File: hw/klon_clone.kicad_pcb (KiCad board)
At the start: 2 copper layers, 0 parts

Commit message: Updated J1/J3 footprints and symbols. Initial layout placement.
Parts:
- added C1: 100n, Capacitor_THT:C_Rect_L13.0mm_W5.0mm_P10.00mm_FKS3_FKP3_MKS4, F.Cu at (118.0, 116.5)
- added C10: 1u, Capacitor_SMD:C_0805_2012Metric_Pad1.18x1.45mm_HandSolder, F.Cu at (181.0, 122.5)
- added C11: 1u, kicad_footprint_library:C_Axial_L17.5mm_W7.8mm_P7.5mm_Horizontal, F.Cu at (130.5, 119.5)
- added C12: 1u, Capacitor_SMD:C_0805_2012Metric_Pad1.18x1.45mm_HandSolder, F.Cu at (172.0, 118.0)
- added C13: 82n, Capacitor_THT:C_Rect_L10.3mm_W5.0mm_P7.50mm_MKS4, F.Cu at (116.3, 102.5)
- added C14: 390p, Capacitor_THT:C_Rect_L10.0mm_W4.0mm_P7.50mm_MKS4, F.Cu at (109.2, 96.5)
- added C15: 1u, kicad_footprint_library:C_Axial_L17.5mm_W7.8mm_P7.5mm_Horizontal, F.Cu at (97.5, 94.5)
- added C16: 47u, Capacitor_THT:CP_Radial_D8.0mm_P5.00mm, F.Cu at (189.1, 104.0)
- added C17: 1u, kicad_footprint_library:C_Axial_L17.5mm_W7.8mm_P7.5mm_Horizontal, F.Cu at (112.0, 84.0)
- added C18: 2.2n, Capacitor_THT:C_Rect_L18.0mm_W7.0mm_P15.00mm_FKS3_FKP3, F.Cu at (119.5, 89.0)
- added C19: 27n, Capacitor_THT:C_Rect_L10.3mm_W4.5mm_P7.50mm_MKS4, F.Cu at (119.5, 82.5)
- added C2: 1u, Capacitor_SMD:C_0805_2012Metric_Pad1.18x1.45mm_HandSolder, F.Cu at (182.0, 102.0)
- added C20: 820p, Capacitor_THT:C_Rect_L13.0mm_W4.0mm_P10.00mm_FKS3_FKP3_MKS4, F.Cu at (119.5, 68.0)
- added C21: 3.9n, Capacitor_THT:C_Rect_L16.5mm_W5.0mm_P15.00mm_MKT, F.Cu at (141.5, 72.0)
- added C22: 4.7u, Capacitor_THT:CP_Radial_D5.0mm_P2.00mm, F.Cu at (146.5, 68.0)
- added C3: 390n, Capacitor_THT:C_Axial_L19.0mm_D9.5mm_P25.00mm_Horizontal, F.Cu at (127.5, 103.0)
- added C4: 68n, Capacitor_THT:C_Axial_L5.1mm_D3.1mm_P15.00mm_Horizontal, F.Cu at (133.0, 113.0)
- added C5: 4.7u, Capacitor_THT:CP_Radial_D5.0mm_P2.00mm, F.Cu at (140.5, 91.0)
- added C6: 47u, Capacitor_THT:CP_Radial_D8.0mm_P5.00mm, F.Cu at (177.4, 100.0)
- added C7: 100n, Capacitor_THT:C_Rect_L13.0mm_W5.0mm_P10.00mm_FKS3_FKP3_MKS4, F.Cu at (95.0, 107.0)
- added C8: 1u, Capacitor_SMD:C_0805_2012Metric_Pad1.18x1.45mm_HandSolder, F.Cu at (172.0, 113.0)
- added C9: 68n, Capacitor_THT:C_Axial_L5.1mm_D3.1mm_P15.00mm_Horizontal, F.Cu at (105.0, 102.0)
- added D1: 1N4742, Diode_THT:D_DO-41_SOD81_P10.16mm_Horizontal, F.Cu at (180.1, 108.0)
- added D2: 1N4001, Diode_THT:D_DO-41_SOD81_P10.16mm_Horizontal, F.Cu at (180.9, 97.5)
- added D3: 1N4001, Diode_THT:D_DO-41_SOD81_P10.16mm_Horizontal, F.Cu at (196.0, 110.4)
- added D4: LED, LED_THT:LED_D5.0mm, F.Cu at (153.7, 79.0)
- added D5: 1N34A, Diode_THT:D_DO-35_SOD27_P10.16mm_Horizontal, F.Cu at (94.4, 88.5)
- added D6: 1N34A, Diode_THT:D_DO-35_SOD27_P10.16mm_Horizontal, F.Cu at (104.6, 85.5)
- added J1: Conn_01x03_Male, Connector_PinHeader_2.54mm:PinHeader_1x03_P2.54mm_Vertical, F.Cu at (105.0, 122.0)
- added J2: Barrel_Jack, Connector_PinHeader_2.54mm:PinHeader_1x02_P2.54mm_Vertical, F.Cu at (190.0, 117.2)
- added J3: Conn_01x03_Male, Connector_PinHeader_2.54mm:PinHeader_1x03_P2.54mm_Vertical, F.Cu at (101.0, 71.5)
- added R1: 10k, Resistor_SMD:R_0805_2012Metric_Pad1.20x1.40mm_HandSolder, F.Cu at (104.0, 118.0)
- added R10: 2k, Resistor_SMD:R_0805_2012Metric_Pad1.20x1.40mm_HandSolder, F.Cu at (121.5, 108.0)
- added R11: 15k, Resistor_SMD:R_0805_2012Metric_Pad1.20x1.40mm_HandSolder, F.Cu at (117.0, 108.0)
- added R12: 15k, Resistor_SMD:R_0805_2012Metric_Pad1.20x1.40mm_HandSolder, F.Cu at (127.5, 113.0)
- added R13: 422k, Resistor_SMD:R_0805_2012Metric_Pad1.20x1.40mm_HandSolder, F.Cu at (109.5, 101.5)
- added R14: 3.9k, Resistor_SMD:R_0805_2012Metric_Pad1.20x1.40mm_HandSolder, F.Cu at (160.5, 79.0)
- added R15: 27k, Resistor_SMD:R_0805_2012Metric_Pad1.20x1.40mm_HandSolder, F.Cu at (184.0, 107.0)
- added R16: 27k, Resistor_SMD:R_0805_2012Metric_Pad1.20x1.40mm_HandSolder, F.Cu at (187.5, 109.5)
- added R17: 1k, Resistor_SMD:R_0805_2012Metric_Pad1.20x1.40mm_HandSolder, F.Cu at (91.0, 88.5)
- added R18: 22k, Resistor_SMD:R_0805_2012Metric_Pad1.20x1.40mm_HandSolder, F.Cu at (126.5, 94.5)
- added R19: 47k, Resistor_SMD:R_0805_2012Metric_Pad1.20x1.40mm_HandSolder, F.Cu at (121.0, 94.5)
- added R2: 1M, Resistor_SMD:R_0805_2012Metric_Pad1.20x1.40mm_HandSolder, F.Cu at (104.0, 115.0)
- added R20: 27k, Resistor_SMD:R_0805_2012Metric_Pad1.20x1.40mm_HandSolder, F.Cu at (123.5, 82.5)
- added R21: 12k, Resistor_SMD:R_0805_2012Metric_Pad1.20x1.40mm_HandSolder, F.Cu at (123.5, 78.0)
- added R22: 392k, Resistor_SMD:R_0805_2012Metric_Pad1.20x1.40mm_HandSolder, F.Cu at (123.5, 74.0)
- added R23: 1.8k, Resistor_SMD:R_0805_2012Metric_Pad1.20x1.40mm_HandSolder, F.Cu at (123.5, 70.0)
- added R24: 100k, Resistor_SMD:R_0805_2012Metric_Pad1.20x1.40mm_HandSolder, F.Cu at (130.5, 83.0)
- added R25: 4.7k, Resistor_SMD:R_0805_2012Metric_Pad1.20x1.40mm_HandSolder, F.Cu at (136.0, 67.5)
- added R26: 100k, Resistor_SMD:R_0805_2012Metric_Pad1.20x1.40mm_HandSolder, F.Cu at (140.5, 78.5)
- added R27: 560, Resistor_SMD:R_0805_2012Metric_Pad1.20x1.40mm_HandSolder, F.Cu at (149.5, 69.0)
- added R28: 68k, Resistor_SMD:R_0805_2012Metric_Pad1.20x1.40mm_HandSolder, F.Cu at (144.5, 73.5)
- added R29: 68k, Resistor_SMD:R_0805_2012Metric_Pad1.20x1.40mm_HandSolder, F.Cu at (148.5, 72.5)
- added R3: 5.1k, Resistor_SMD:R_0805_2012Metric_Pad1.20x1.40mm_HandSolder, F.Cu at (127.0, 109.5)
- added R30: 100k, Resistor_SMD:R_0805_2012Metric_Pad1.20x1.40mm_HandSolder, F.Cu at (153.0, 86.0)
- added R4: 1.5k, Resistor_SMD:R_0805_2012Metric_Pad1.20x1.40mm_HandSolder, F.Cu at (137.0, 109.5)
- added R5: 1k, Resistor_SMD:R_0805_2012Metric_Pad1.20x1.40mm_HandSolder, F.Cu at (141.5, 109.5)
- added R6: 100k, Resistor_SMD:R_0805_2012Metric_Pad1.20x1.40mm_HandSolder, F.Cu at (141.5, 86.0)
- added R7: 560, Resistor_SMD:R_0805_2012Metric_Pad1.20x1.40mm_HandSolder, F.Cu at (141.5, 83.0)
- added R8: 1.5k, Resistor_SMD:R_0805_2012Metric_Pad1.20x1.40mm_HandSolder, F.Cu at (100.0, 110.5)
- added R9: 10k, Resistor_SMD:R_0805_2012Metric_Pad1.20x1.40mm_HandSolder, F.Cu at (100.0, 106.0)
- added RV1: 100k, Connector_PinHeader_2.54mm:PinHeader_1x03_P2.54mm_Vertical, F.Cu at (135.5, 95.0)
- added RV2: 100k, Connector_PinHeader_2.54mm:PinHeader_1x03_P2.54mm_Vertical, F.Cu at (122.0, 111.5)
- added RV3: 10k, Connector_PinHeader_2.54mm:PinHeader_1x03_P2.54mm_Vertical, F.Cu at (127.0, 67.5)
- added RV4: 10k, Connector_PinHeader_2.54mm:PinHeader_1x03_P2.54mm_Vertical, F.Cu at (153.5, 68.5)
- added SW1: SW_DPDT_x2, Connector_PinHeader_2.54mm:PinHeader_1x06_P2.54mm_Vertical, F.Cu at (148.5, 75.7)
- added U1: TL072, Package_SO:SO-8_5.3x6.2mm_P1.27mm, F.Cu at (108.5, 109.0)
- added U2: ICL7660, Package_SO:SO-8_5.3x6.2mm_P1.27mm, F.Cu at (180.5, 115.0)
- added U3: TL072, Package_SO:SO-8_5.3x6.2mm_P1.27mm, F.Cu at (130.5, 78.5)
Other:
- board outline added: 112 x 60 mm
- net class Default removed

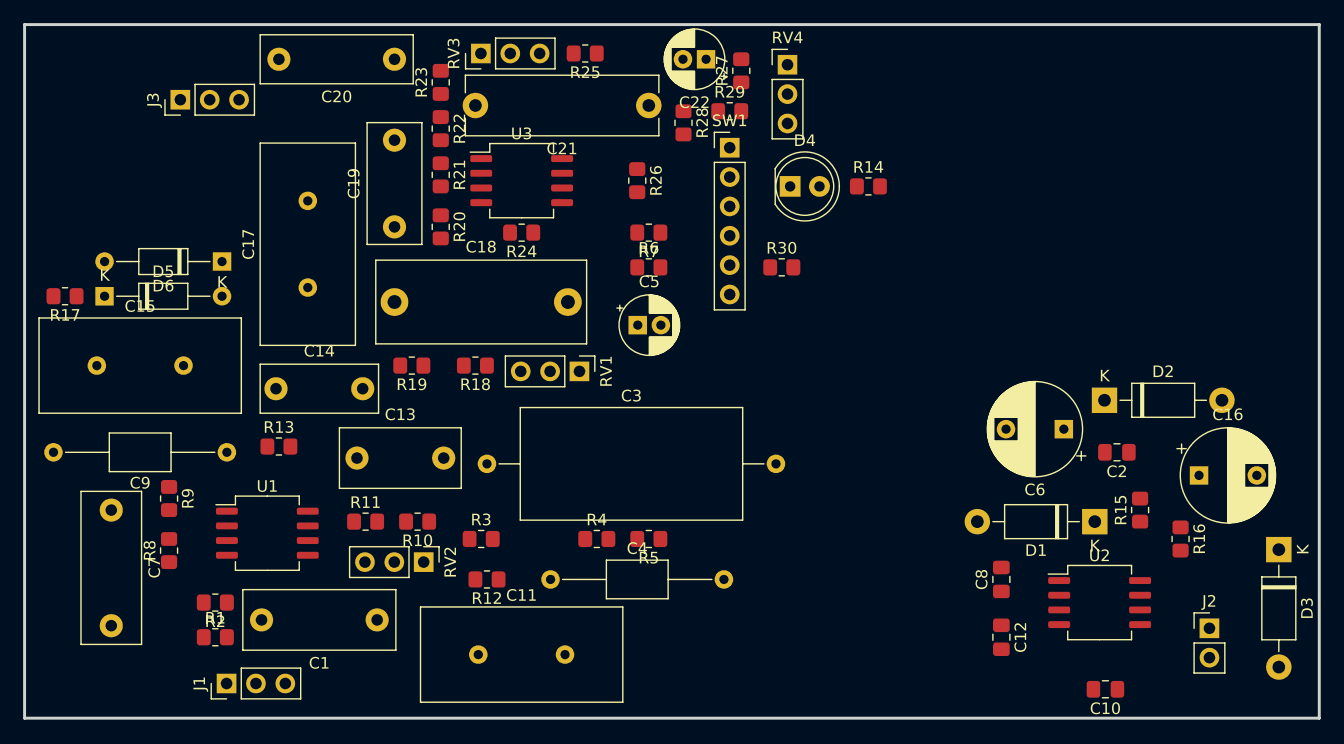
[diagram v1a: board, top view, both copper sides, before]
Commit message: Layout Updates
Started routing traces on layer 1
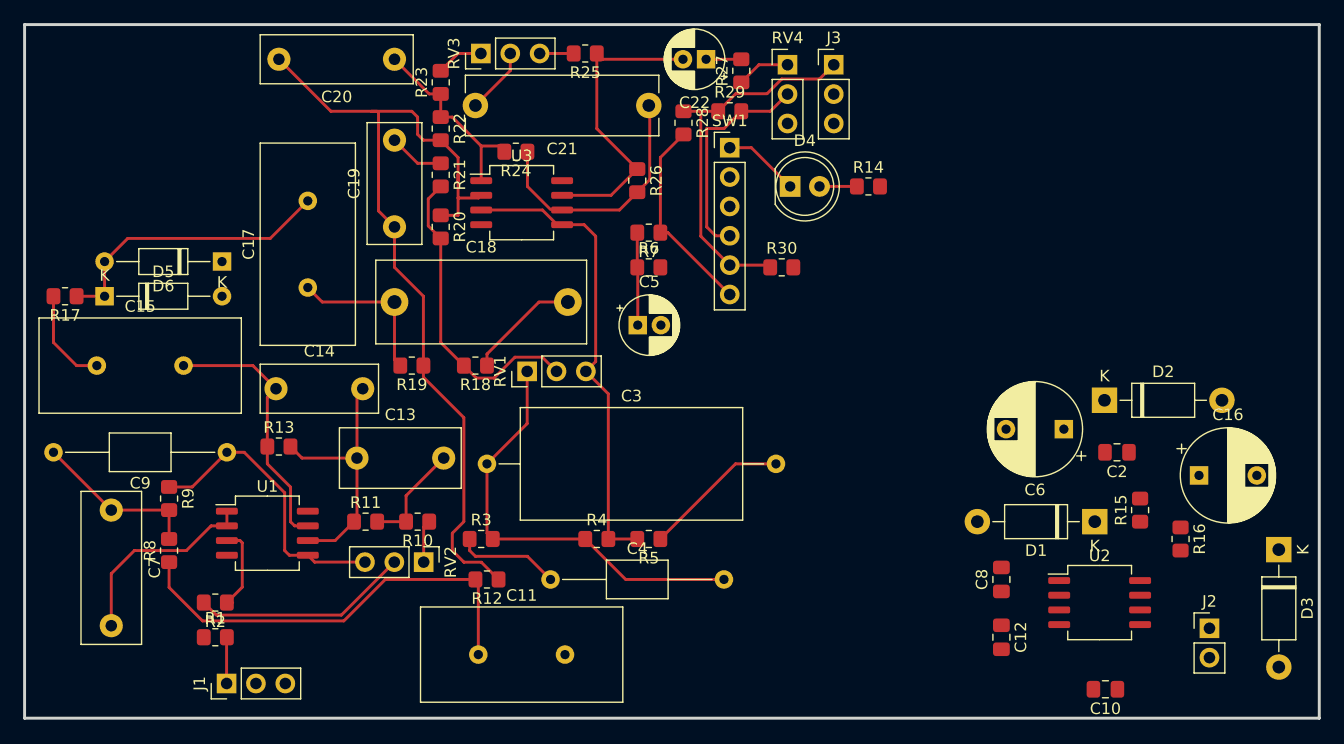
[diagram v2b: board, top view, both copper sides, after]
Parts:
- removed C1: 100n, Capacitor_THT:C_Rect_L13.0mm_W5.0mm_P10.00mm_FKS3_FKP3_MKS4
- moved J3 56.6 mm to (157.5, 68.5), turned to 0 degrees
- moved R24 7.02 mm to (130.0, 76.0)
- moved RV1 4.53 mm to (131.0, 95.0), turned to 90 degrees
- moved U3 1.91 mm to (130.5, 80.4)
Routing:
- net Net-(C19-Pad1): track 0.00 -> 76.2 mm
- net +4V5: track 0.00 -> 59.5 mm
- net Net-(C11-Pad1): track 0.00 -> 38.0 mm
- net Net-(C3-Pad1): track 0.00 -> 37.6 mm
- net Net-(R28-Pad1): track 0.00 -> 32.6 mm
- net Net-(R18-Pad2): track 0.00 -> 26.9 mm
- net Net-(C4-Pad1): track 0.00 -> 26.7 mm
- net Net-(C22-Pad2): track 0.00 -> 26.6 mm
- net Net-(C17-Pad2): track 0.00 -> 25.2 mm
- net Net-(C9-Pad1): track 0.00 -> 25.1 mm
- net Net-(C14-Pad1): track 0.00 -> 23.1 mm
- net Net-(C13-Pad1): track 0.00 -> 22.7 mm
- net Net-(C21-Pad1): track 0.00 -> 21.5 mm
- net Net-(R29-Pad2): track 0.00 -> 19.0 mm
- net Net-(R28-Pad2): track 0.00 -> 17.5 mm
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
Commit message: PCB Updates
Almost completed board. FInished traces, poured GND plane on layer2, added names and mounting holes.
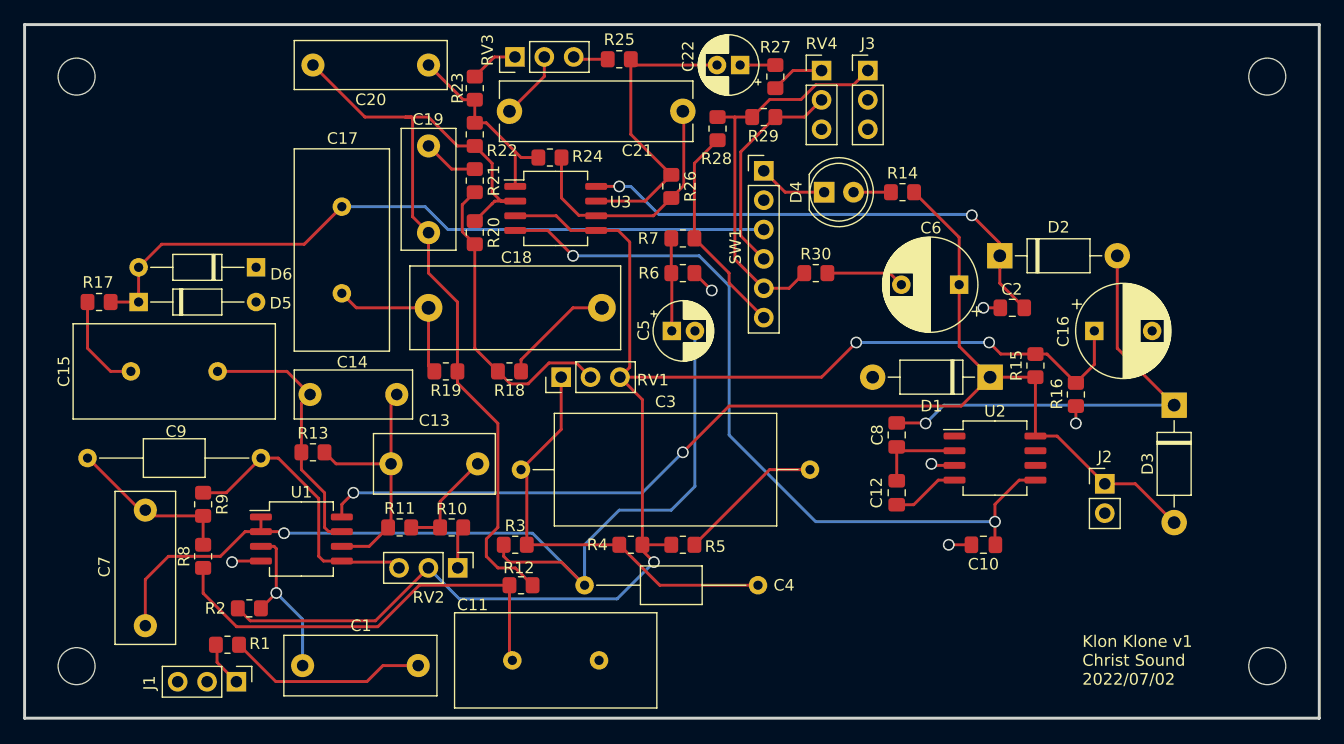
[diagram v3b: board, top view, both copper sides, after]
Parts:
- added C1: 100n, Capacitor_THT:C_Rect_L13.0mm_W5.0mm_P10.00mm_FKS3_FKP3_MKS4, F.Cu at (111.5, 120.5)
- added J4: Conn_01x01_Female, MountingHole:MountingHole_3.2mm_M3, F.Cu at (195.0, 120.5)
- added J5: Conn_01x01_Female, MountingHole:MountingHole_3.2mm_M3, F.Cu at (195.0, 69.5)
- added J6: Conn_01x01_Female, MountingHole:MountingHole_3.2mm_M3, F.Cu at (92.0, 69.5)
- added J7: Conn_01x01_Female, MountingHole:MountingHole_3.2mm_M3, F.Cu at (92.0, 120.5)
- moved C10 16.4 mm to (170.4, 110.0)
- moved C12 15.4 mm to (162.9, 105.5)
- moved C16 15.4 mm to (180.0, 91.5)
- moved C2 15.4 mm to (172.9, 89.5)
- moved C8 15.4 mm to (162.9, 100.5)
- moved D1 15.4 mm to (171.0, 95.5)
- moved D3 15.4 mm to (186.9, 97.9)
- moved J2 15.4 mm to (180.9, 104.7)
- moved R15 15.4 mm to (174.9, 94.5)
- moved R16 15.4 mm to (178.4, 97.0)
- moved U2 15.4 mm to (171.4, 102.5)
- moved C6 15.4 mm to (168.3, 87.5)
- moved D2 15.4 mm to (171.9, 85.0)
- moved SW1 3.56 mm to (151.4, 77.7)
- moved C5 2.99 mm to (143.5, 91.5)
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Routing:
- net +9V: track 0.00 -> 104.6 mm, vias 0 -> 2
- net +4V5: track 59.5 -> 130.7 mm, vias 0 -> 3
- net -8V6: track 0.00 -> 67.4 mm, vias 0 -> 2
- net Net-(C4-Pad1): track 26.7 -> 84.5 mm, vias 0 -> 1
- net +16V2: track 0.00 -> 43.4 mm, vias 0 -> 2
- net Net-(C8-Pad2): track 0.00 -> 39.6 mm, vias 0 -> 1
- net Net-(C17-Pad2): track 25.2 -> 62.5 mm
- net Earth: track 0.00 -> 18.5 mm, vias 0 -> 6
- net Net-(C1-Pad2): track 0.00 -> 17.4 mm
- net Net-(C12-Pad1): track 0.00 -> 8.06 mm
- net Net-(C1-Pad1): track 7.63 -> 14.4 mm, vias 0 -> 1
- net Net-(C12-Pad2): track 0.00 -> 5.88 mm
- net Net-(J3-Pad1): track 32.6 -> 34.6 mm
- net Net-(C19-Pad1): track 76.2 -> 75.1 mm
- net Net-(R28-Pad2): track 17.5 -> 18.7 mm
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- added copper zone on B.Cu, net Earth
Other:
- board text added: "Klon Klone v1 Christ Sound 2022/07/02"
